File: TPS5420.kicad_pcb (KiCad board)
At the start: 2 copper layers, 25.5 x 19.9 mm, 10 parts, among them U1 TPS5420D, U2 CDBC560-G

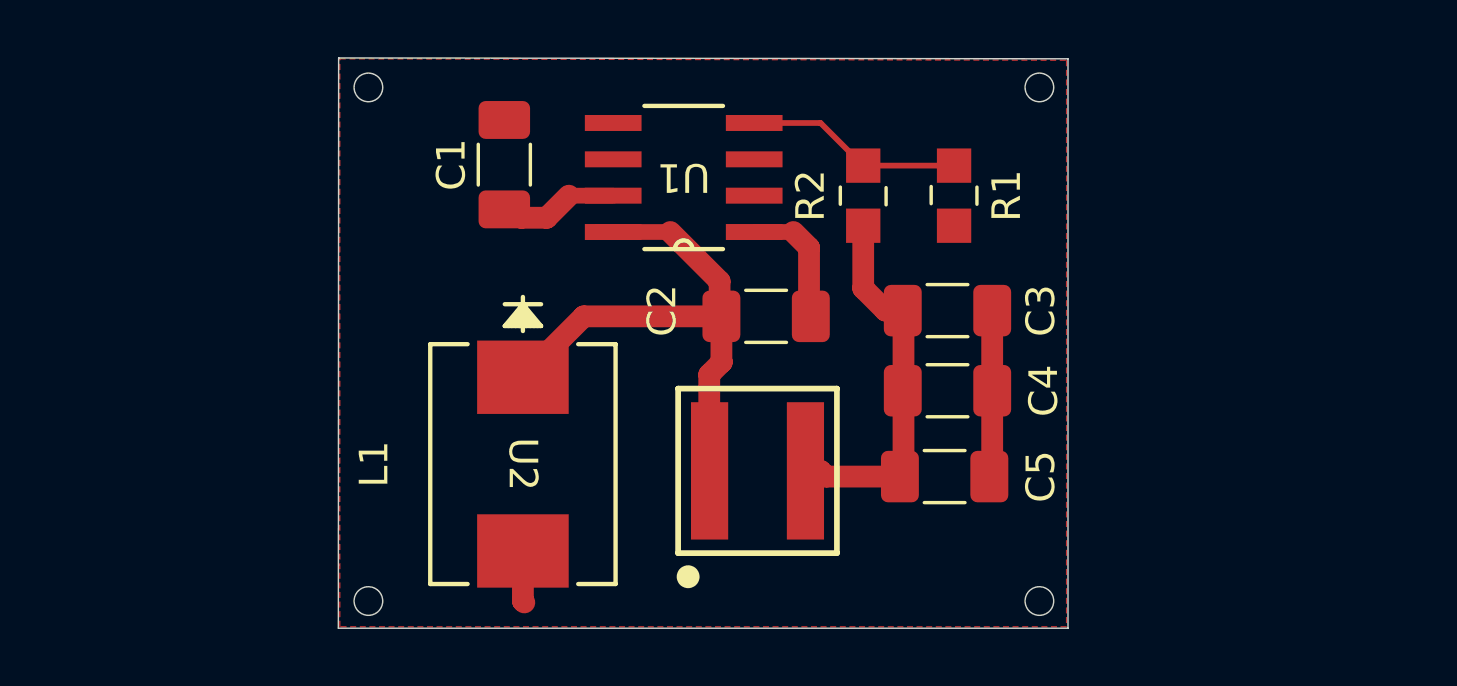
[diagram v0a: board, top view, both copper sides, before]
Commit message: Added scre terminals
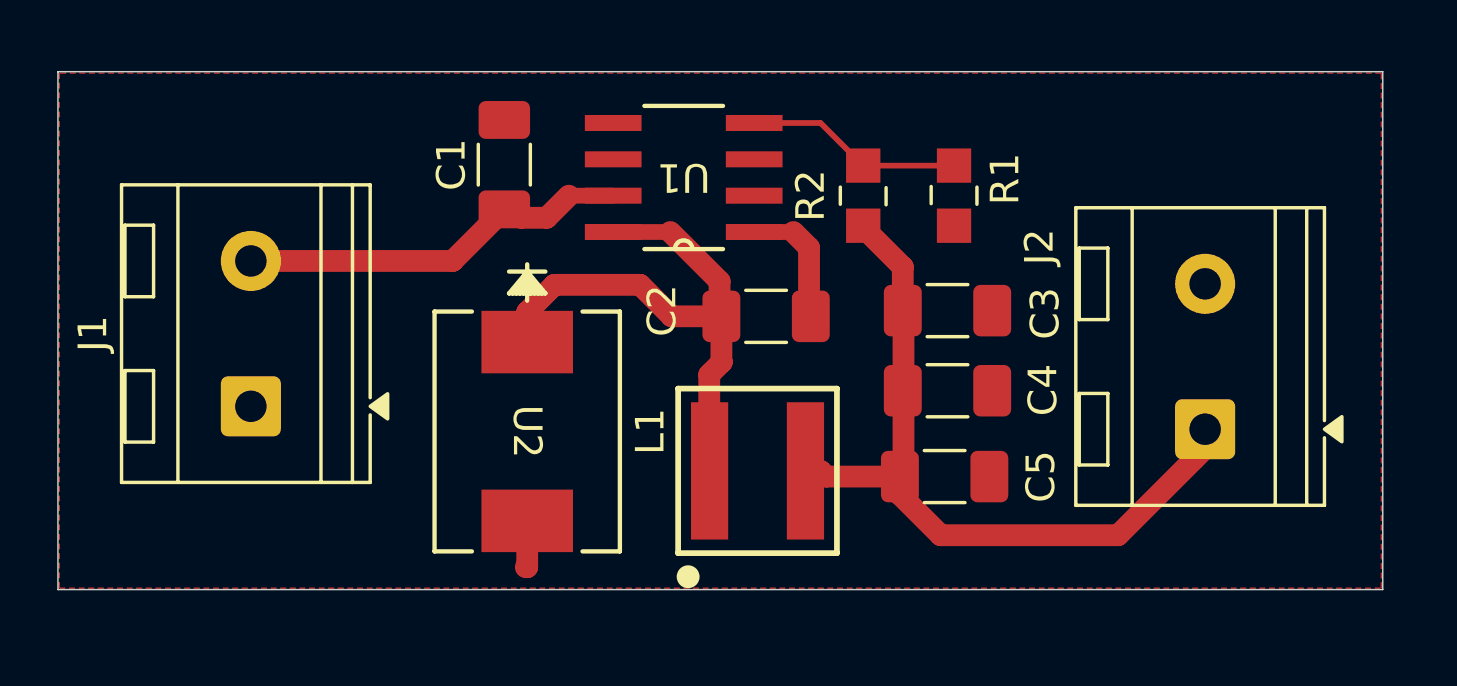
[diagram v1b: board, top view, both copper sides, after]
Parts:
- added J1: Screw_Terminal_01x02, TerminalBlock_RND:TerminalBlock_RND_205-00232_1x02_P5.08mm_Horizontal, F.Cu at (121.4, 89.6)
- added J2: Screw_Terminal_01x02, TerminalBlock_RND:TerminalBlock_RND_205-00232_1x02_P5.08mm_Horizontal, F.Cu at (154.7, 90.4)
- U2: footprint TPS5420_CADs:CDBC-G-M -> TPS5420_CADs:CDBC-G
- moved U2 1.15 mm to (131.1, 90.5)
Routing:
- net /Vout: track 13.2 -> 27.6 mm
- net Net-(J1-Pin_2): track 4.70 -> 14.3 mm
- net GND: track 8.30 -> 2.45 mm
- net Net-(U1-PH): track 20.0 -> 21.7 mm
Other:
- board size 25.5 x 19.9 mm -> 46.3 x 18.1 mm

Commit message: v-03 Added ground pour and vias
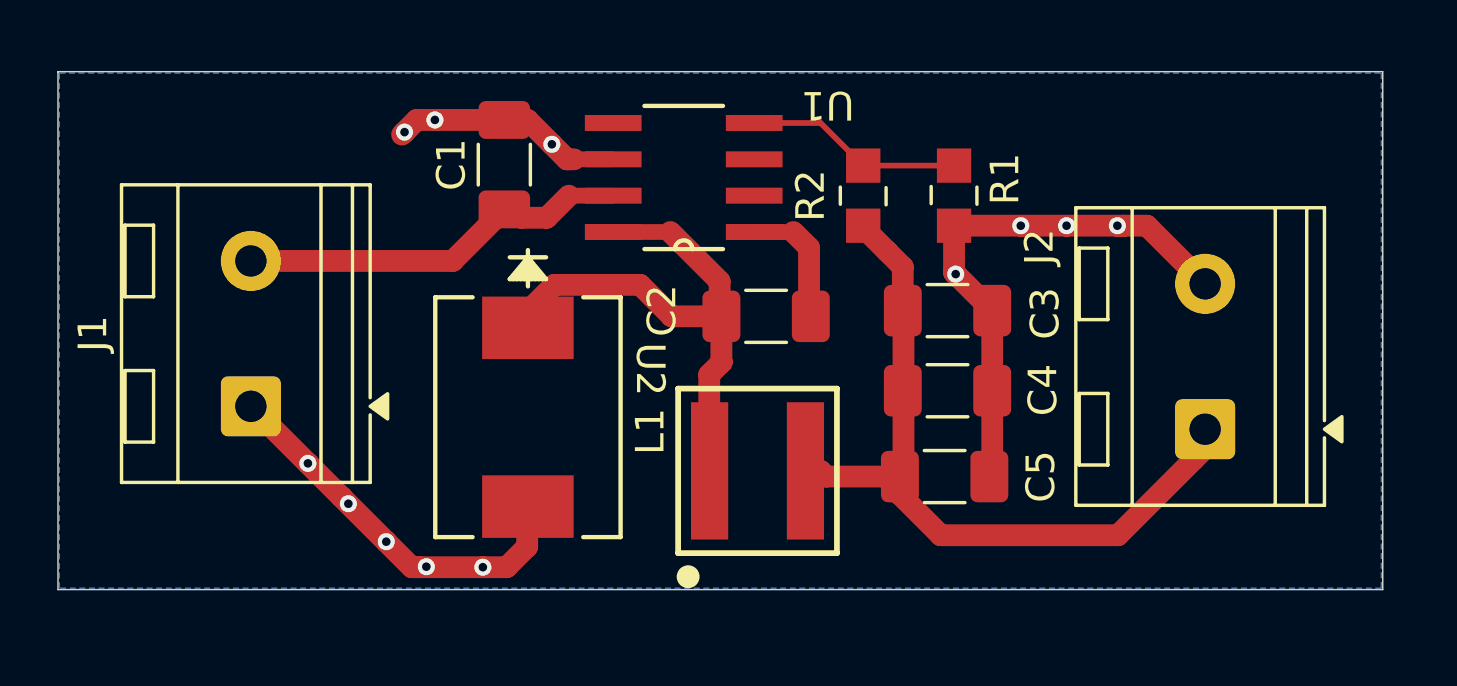
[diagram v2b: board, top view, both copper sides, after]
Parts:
- moved U2 0.50 mm to (131.1, 90.0)
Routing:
- net GND: track 2.45 -> 40.5 mm, vias 0 -> 12
- net Net-(U1-PH): track 21.7 -> 20.9 mm
- added copper zone on B.Cu, net GND
- removed copper zone on F.Cu, net GND

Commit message: v
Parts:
- moved J2 5.19 mm to (154.7, 85.3), turned to -90 degrees
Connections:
- J2 pad 1: /Vout -> GND
- J2 pad 2: GND -> /Vout
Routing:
- net GND: track 40.5 -> 6.87 mm, vias 12 -> 33
- added copper zone on F.Cu, net GND
